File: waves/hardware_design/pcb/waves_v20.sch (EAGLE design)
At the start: 110 parts, among them IC1 PCM5100PW, IC10 LD2981ABU33TR, IC2 STM32F405RGT6, IC3 1-2199298-2, IC4 1-2199298-2, IC5 MCP6004T-I_SL, IC7 TL072CD, IC8 LM4040C10IDBZR, IC9 LM1117DT-3.3_NOPB, J1 PJ301_THONKICONN6, J2 PJ301_THONKICONN6, J3 PJ301_THONKICONN6, J4 PJ301_THONKICONN6, J5 PJ301_THONKICONN6, J6 PJ301_THONKICONN6, J8 F31L-1A7H1-11030, Q1 CRYSTAL, U1 PEC11R-4215F-S0024

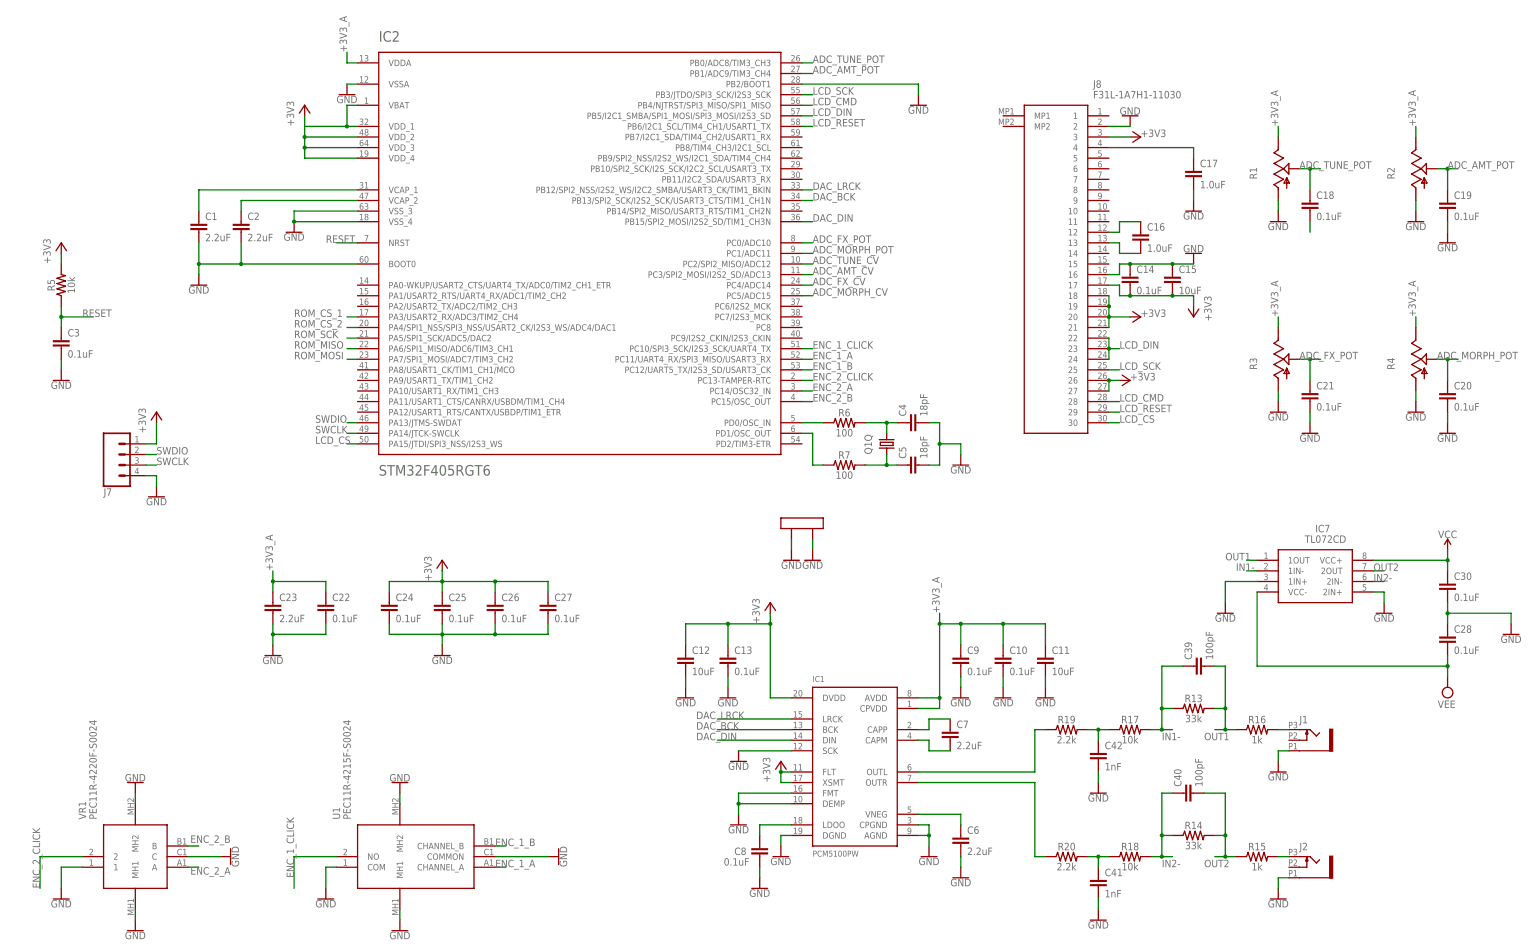
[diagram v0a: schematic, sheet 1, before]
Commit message: schematic changes. handle +/- 10 volts. 0-8v for pitch
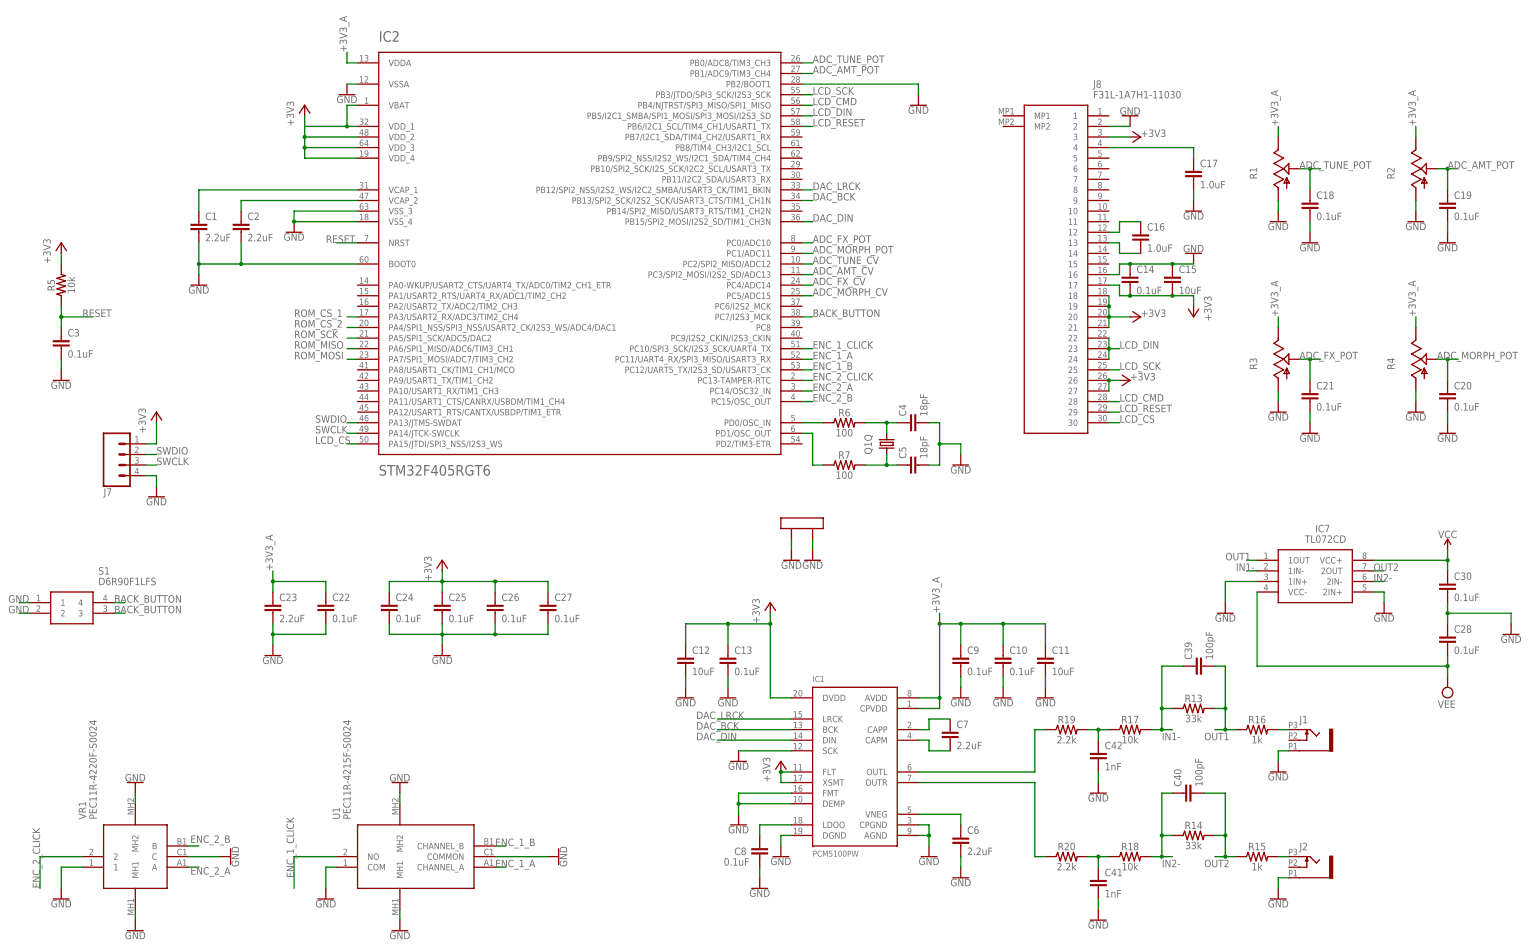
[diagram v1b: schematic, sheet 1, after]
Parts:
- removed R30: 100k, SparkFun-Resistors:100KOHM-0603-1/10W-1%
- added S1: D6R90F1LFS, D6R Push Button:D6R90F1LFS
- R21: value 100k -> 80.6k; device SparkFun-Resistors:100KOHM-0603-1/10W-1% -> SparkFun-Resistors:82OHM-0603-1/10W-1%
- R24, R27: value 100k -> 200k; device SparkFun-Resistors:100KOHM-0603-1/10W-1% -> SparkFun-Resistors:200KOHM-0603-1/10W-1%
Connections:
- removed net N$28: C18.2
- new net BACK_BUTTON: IC2.PC7/I2S3_MCK, S1.3, S1.4
- net AREF_-10: no longer R22.1
- net GND: now also C18.2, S1.1, S1.2
- net N$23: now also R22.1; no longer R30.1
- net VINA-: no longer R22.2
- net VIND-: now also R22.2; no longer R30.2
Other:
- moved on the sheet: R22

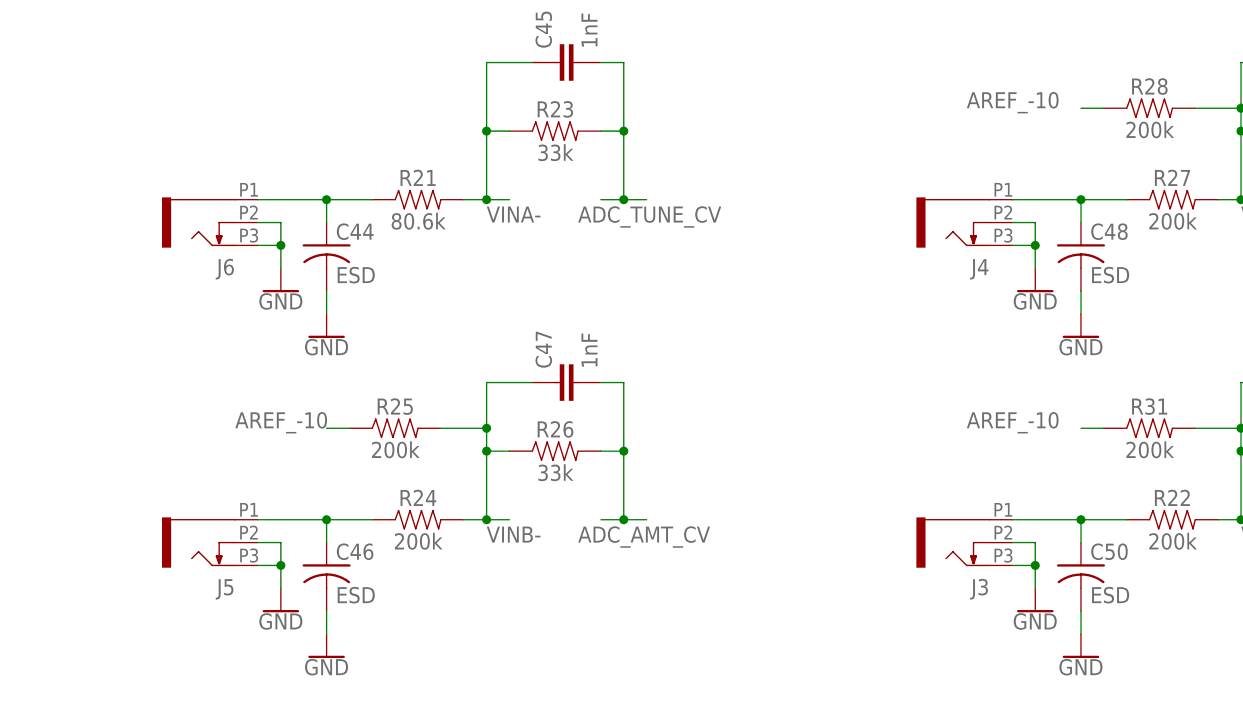
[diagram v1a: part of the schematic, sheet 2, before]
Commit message: progress on audio DAC. switched to f446xx for now
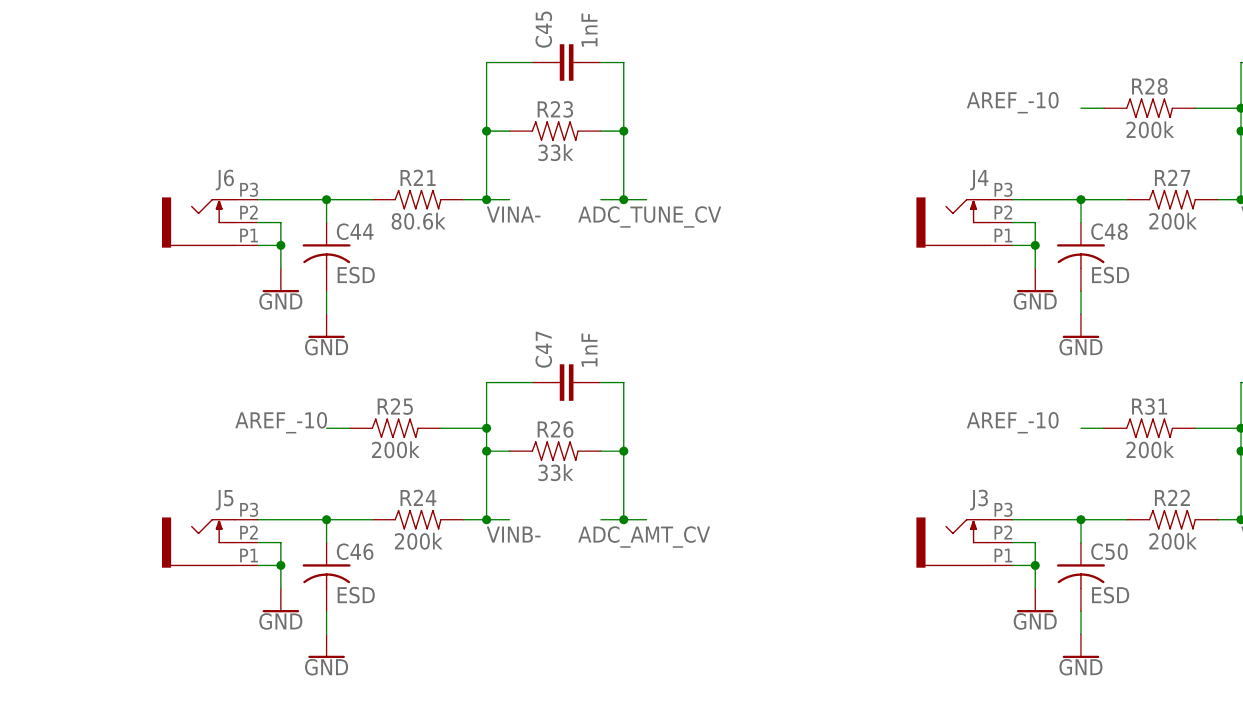
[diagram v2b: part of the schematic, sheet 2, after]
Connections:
- net GND: now also J3.1, J4.1, J5.1, J6.1; no longer J3.3, J4.3, J5.3, J6.3
- net N$15: now also J5.3; no longer J5.1
- net N$16: now also J6.3; no longer J6.1
- net N$17: now also J4.3; no longer J4.1
- net N$23: now also J3.3; no longer J3.1
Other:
- moved on the sheet: J3, J4, J5, J6
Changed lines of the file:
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@@
 <attribute name="VALUE" x="77.47" y="127" size="1.778" layer="96" align="center-left"/>
 </instance>
-<instance part="J3" gate="G$1" x="241.3" y="68.58" smashed="yes" rot="R180">
-<attribute name="NAME" x="243.84" y="64.516" size="1.778" layer="95" rot="R180"/>
-</instance>
-<instance part="J4" gate="G$1" x="241.3" y="104.14" smashed="yes" rot="R180">
-<attribute name="NAME" x="243.84" y="100.076" size="1.778" layer="95" rot="R180"/>
+<instance part="J3" gate="G$1" x="241.3" y="68.58" smashed="yes" rot="MR0">
+<attribute name="NAME" x="243.84" y="72.644" size="1.778" layer="95" rot="MR0"/>
+</instance>
+<instance part="J4" gate="G$1" x="241.3" y="104.14" smashed="yes" rot="MR0">
+<attribute name="NAME" x="243.84" y="108.204" size="1.778" layer="95" rot="MR0"/>
 </instance>
 <instance part="+3V10" gate="G$1" x="347.98" y="198.12" smashed="yes">
@@
 <attribute name="VALUE" x="314.96" y="170.18" size="1.778" layer="96" rot="R270"/>
 </instance>
-<instance part="J5" gate="G$1" x="157.48" y="68.58" smashed="yes" rot="R180">
-<attribute name="NAME" x="160.02" y="64.516" size="1.778" layer="95" rot="R180"/>
-</instance>
-<instance part="J6" gate="G$1" x="157.48" y="104.14" smashed="yes" rot="R180">
-<attribute name="NAME" x="160.02" y="100.076" size="1.778" layer="95" rot="R180"/>
+<instance part="J5" gate="G$1" x="157.48" y="68.58" smashed="yes" rot="MR0">
+<attribute name="NAME" x="160.02" y="72.644" size="1.778" layer="95" rot="MR0"/>
+</instance>
+<instance part="J6" gate="G$1" x="157.48" y="104.14" smashed="yes" rot="MR0">
+<attribute name="NAME" x="160.02" y="108.204" size="1.778" layer="95" rot="MR0"/>
 </instance>
 <instance part="JP1" gate="A" x="35.56" y="187.96" smashed="yes">
@@
 </segment>
 <segment>
+<wire x1="165.1" y1="104.14" x2="165.1" y2="101.6" width="0.1524" layer="91"/>
+<pinref part="GND60" gate="1" pin="GND"/>
 <pinref part="J6" gate="G$1" pin="2"/>
+<wire x1="165.1" y1="101.6" x2="165.1" y2="99.06" width="0.1524" layer="91"/>
 <wire x1="162.56" y1="104.14" x2="165.1" y2="104.14" width="0.1524" layer="91"/>
-<wire x1="165.1" y1="104.14" x2="165.1" y2="101.6" width="0.1524" layer="91"/>
-<pinref part="J6" gate="G$1" pin="3"/>
-<wire x1="165.1" y1="101.6" x2="162.56" y2="101.6" width="0.1524" layer="91"/>
-<wire x1="165.1" y1="101.6" x2="165.1" y2="99.06" width="0.1524" layer="91"/>
+<pinref part="J6" gate="G$1" pin="1"/>
+<wire x1="162.56" y1="101.6" x2="165.1" y2="101.6" width="0.1524" layer="91"/>
 <junction x="165.1" y="101.6"/>
-<pinref part="GND60" gate="1" pin="GND"/>
 </segment>
 <segment>
@@
 </segment>
 <segment>
+<wire x1="165.1" y1="68.58" x2="165.1" y2="66.04" width="0.1524" layer="91"/>
+<pinref part="GND66" gate="1" pin="GND"/>
 <pinref part="J5" gate="G$1" pin="2"/>
+<wire x1="165.1" y1="66.04" x2="165.1" y2="63.5" width="0.1524" layer="91"/>
 <wire x1="162.56" y1="68.58" x2="165.1" y2="68.58" width="0.1524" layer="91"/>
-<wire x1="165.1" y1="68.58" x2="165.1" y2="66.04" width="0.1524" layer="91"/>
-<pinref part="J5" gate="G$1" pin="3"/>
-<wire x1="165.1" y1="66.04" x2="162.56" y2="66.04" width="0.1524" layer="91"/>
-<wire x1="165.1" y1="66.04" x2="165.1" y2="63.5" width="0.1524" layer="91"/>
+<pinref part="J5" gate="G$1" pin="1"/>
+<wire x1="162.56" y1="66.04" x2="165.1" y2="66.04" width="0.1524" layer="91"/>
 <junction x="165.1" y="66.04"/>
-<pinref part="GND66" gate="1" pin="GND"/>
-</segment>
-<segment>
+</segment>
+<segment>
+<wire x1="248.92" y1="68.58" x2="248.92" y2="66.04" width="0.1524" layer="91"/>
+<pinref part="GND67" gate="1" pin="GND"/>
 <pinref part="J3" gate="G$1" pin="2"/>
+<wire x1="248.92" y1="66.04" x2="248.92" y2="63.5" width="0.1524" layer="91"/>
 <wire x1="246.38" y1="68.58" x2="248.92" y2="68.58" width="0.1524" layer="91"/>
-<wire x1="248.92" y1="68.58" x2="248.92" y2="66.04" width="0.1524" layer="91"/>
-<pinref part="J3" gate="G$1" pin="3"/>
-<wire x1="248.92" y1="66.04" x2="246.38" y2="66.04" width="0.1524" layer="91"/>
-<wire x1="248.92" y1="66.04" x2="248.92" y2="63.5" width="0.1524" layer="91"/>
+<pinref part="J3" gate="G$1" pin="1"/>
+<wire x1="246.38" y1="66.04" x2="248.92" y2="66.04" width="0.1524" layer="91"/>
 <junction x="248.92" y="66.04"/>
-<pinref part="GND67" gate="1" pin="GND"/>
-</segment>
-<segment>
+</segment>
+<segment>
+<wire x1="248.92" y1="104.14" x2="248.92" y2="101.6" width="0.1524" layer="91"/>
+<pinref part="GND68" gate="1" pin="GND"/>
 <pinref part="J4" gate="G$1" pin="2"/>
+<wire x1="248.92" y1="101.6" x2="248.92" y2="99.06" width="0.1524" layer="91"/>
 <wire x1="246.38" y1="104.14" x2="248.92" y2="104.14" width="0.1524" layer="91"/>
-<wire x1="248.92" y1="104.14" x2="248.92" y2="101.6" width="0.1524" layer="91"/>
-<pinref part="J4" gate="G$1" pin="3"/>
-<wire x1="248.92" y1="101.6" x2="246.38" y2="101.6" width="0.1524" layer="91"/>
-<wire x1="248.92" y1="101.6" x2="248.92" y2="99.06" width="0.1524" layer="91"/>
+<pinref part="J4" gate="G$1" pin="1"/>
+<wire x1="246.38" y1="101.6" x2="248.92" y2="101.6" width="0.1524" layer="91"/>
 <junction x="248.92" y="101.6"/>
-<pinref part="GND68" gate="1" pin="GND"/>
 </segment>
 </net>
@@
 <net name="N$16" class="0">
 <segment>
-<pinref part="J6" gate="G$1" pin="1"/>
-<wire x1="162.56" y1="106.68" x2="170.18" y2="106.68" width="0.1524" layer="91"/>
-<junction x="170.18" y="106.68"/>
 <wire x1="170.18" y1="106.68" x2="170.18" y2="104.14" width="0.1524" layer="91"/>
 <pinref part="C44" gate="G$1" pin="1"/>
 <wire x1="170.18" y1="106.68" x2="175.26" y2="106.68" width="0.1524" layer="91"/>
 <pinref part="R21" gate="G$1" pin="1"/>
+<pinref part="J6" gate="G$1" pin="3"/>
+<wire x1="162.56" y1="106.68" x2="170.18" y2="106.68" width="0.1524" layer="91"/>
+<junction x="170.18" y="106.68"/>
 </segment>
 </net>
@@
 <net name="N$15" class="0">
 <segment>
-<wire x1="162.56" y1="71.12" x2="170.18" y2="71.12" width="0.1524" layer="91"/>
-<junction x="170.18" y="71.12"/>
 <wire x1="170.18" y1="71.12" x2="170.18" y2="68.58" width="0.1524" layer="91"/>
 <pinref part="C46" gate="G$1" pin="1"/>
 <wire x1="170.18" y1="71.12" x2="175.26" y2="71.12" width="0.1524" layer="91"/>
-<pinref part="J5" gate="G$1" pin="1"/>
 <pinref part="R24" gate="G$1" pin="1"/>
+<pinref part="J5" gate="G$1" pin="3"/>
+<wire x1="162.56" y1="71.12" x2="170.18" y2="71.12" width="0.1524" layer="91"/>
+<junction x="170.18" y="71.12"/>
 </segment>
 </net>
@@
 <pinref part="C48" gate="G$1" pin="1"/>
 <wire x1="254" y1="106.68" x2="259.08" y2="106.68" width="0.1524" layer="91"/>
-<pinref part="J4" gate="G$1" pin="1"/>
-<wire x1="254" y1="106.68" x2="246.38" y2="106.68" width="0.1524" layer="91"/>
+<pinref part="R27" gate="G$1" pin="1"/>
+<pinref part="J4" gate="G$1" pin="3"/>
+<wire x1="246.38" y1="106.68" x2="254" y2="106.68" width="0.1524" layer="91"/>
 <junction x="254" y="106.68"/>
-<pinref part="R27" gate="G$1" pin="1"/>
 </segment>
 </net>
 <net name="N$23" class="0">
 <segment>
-<wire x1="246.38" y1="71.12" x2="254" y2="71.12" width="0.1524" layer="91"/>
-<junction x="254" y="71.12"/>
 <wire x1="254" y1="71.12" x2="254" y2="68.58" width="0.1524" layer="91"/>
 <pinref part="C50" gate="G$1" pin="1"/>
 <wire x1="254" y1="71.12" x2="259.08" y2="71.12" width="0.1524" layer="91"/>
-<pinref part="J3" gate="G$1" pin="1"/>
 <pinref part="R22" gate="G$1" pin="1"/>
-</segment>
-</net>
+<pinref part="J3" gate="G$1" pin="3"/>
+<wire x1="246.38" y1="71.12" x2="254" y2="71.12" width="0.1524" layer="91"/>
+<junction x="254" y="71.12"/>
+</segment>
+</net>

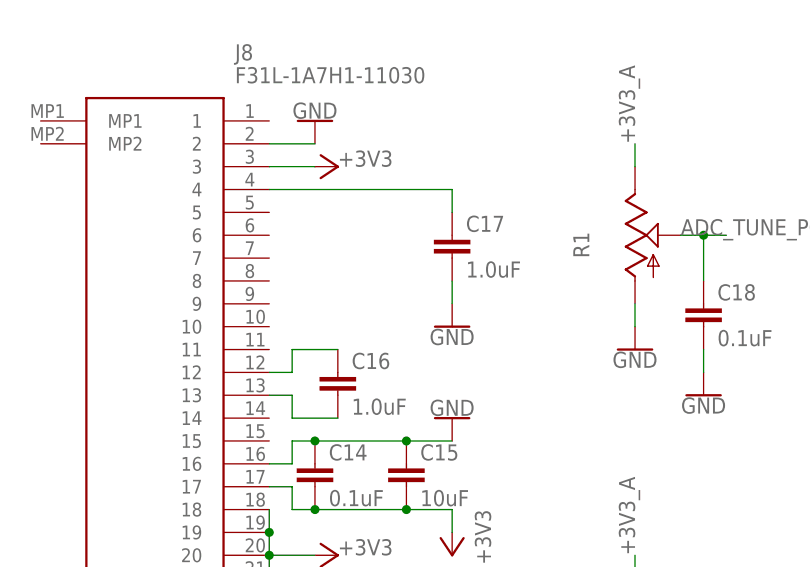
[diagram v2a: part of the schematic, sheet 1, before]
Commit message: starting to add xcode wavetable code
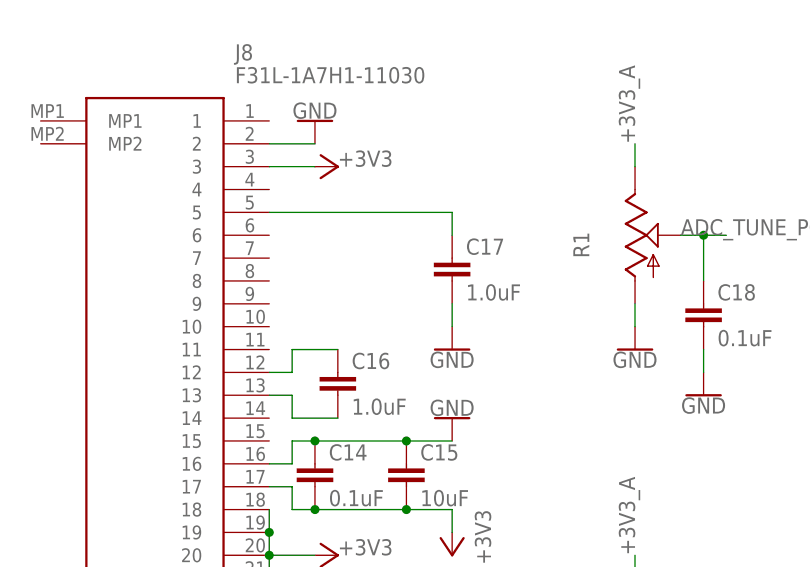
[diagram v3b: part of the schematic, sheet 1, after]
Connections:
- net N$3: now also J8.5; no longer J8.4
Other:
- moved on the sheet: C17
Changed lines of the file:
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@@
 <attribute name="VALUE" x="289.56" y="213.36" size="1.778" layer="96"/>
 </instance>
-<instance part="C17" gate="G$1" x="302.26" y="203.2" smashed="yes">
-<attribute name="NAME" x="303.784" y="206.121" size="1.778" layer="95" font="vector"/>
-<attribute name="VALUE" x="303.784" y="201.041" size="1.778" layer="96" font="vector"/>
-</instance>
-<instance part="GND25" gate="1" x="302.26" y="195.58" smashed="yes">
-<attribute name="VALUE" x="302.26" y="195.326" size="1.778" layer="96" align="top-center"/>
+<instance part="C17" gate="G$1" x="302.26" y="200.66" smashed="yes">
+<attribute name="NAME" x="303.784" y="203.581" size="1.778" layer="95" font="vector"/>
+<attribute name="VALUE" x="303.784" y="198.501" size="1.778" layer="96" font="vector"/>
+</instance>
+<instance part="GND25" gate="1" x="302.26" y="193.04" smashed="yes">
+<attribute name="VALUE" x="302.26" y="192.786" size="1.778" layer="96" align="top-center"/>
 </instance>
 <instance part="C16" gate="G$1" x="289.56" y="187.96" smashed="yes">
@@
 <pinref part="C17" gate="G$1" pin="2"/>
 <pinref part="GND25" gate="1" pin="GND"/>
-<wire x1="302.26" y1="198.12" x2="302.26" y2="200.66" width="0.1524" layer="91"/>
+<wire x1="302.26" y1="195.58" x2="302.26" y2="198.12" width="0.1524" layer="91"/>
 </segment>
 <segment>
@@
 </segment>
 </net>
-<net name="N$3" class="0">
-<segment>
-<pinref part="J8" gate="G$1" pin="4"/>
-<wire x1="281.94" y1="210.82" x2="302.26" y2="210.82" width="0.1524" layer="91"/>
-<wire x1="302.26" y1="210.82" x2="302.26" y2="208.28" width="0.1524" layer="91"/>
-<pinref part="C17" gate="G$1" pin="1"/>
-</segment>
-</net>
 <net name="N$12" class="0">
 <segment>
@@
 </segment>
 </net>
+<net name="N$3" class="0">
+<segment>
+<pinref part="J8" gate="G$1" pin="5"/>
+<wire x1="281.94" y1="208.28" x2="302.26" y2="208.28" width="0.1524" layer="91"/>
+<pinref part="C17" gate="G$1" pin="1"/>
+<wire x1="302.26" y1="208.28" x2="302.26" y2="205.74" width="0.1524" layer="91"/>
+</segment>
+</net>
